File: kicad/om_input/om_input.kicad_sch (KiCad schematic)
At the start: 59 parts, among them J2 XLR3_AudioJack3_Combo_Switch, J3 Conn_01x08_Pin, Q1 PNP, Q2 PNP, SW1 SW_DPDT_x2, SW2 SW_4PDT_x4, U1 OPA1641, U2 OPA1612AxD, U3 OPA1612AxD, U4 OPA1612AxD, U5 OPA1612AxD

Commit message: gain and rails (#4)
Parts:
- added R28, R29, R30, R31: 1k, symbol Device:R_US
- R23: value 270 -> 100
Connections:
- net -9V: no longer D2.2 (A), D5.2 (A), J3.4 (Pin_4), R10.2, R15.2, U2.4 (V-), U4.4 (V-), U5.4 (V-)
- net Earth: now also R28.2, R29.1
- net at U3.1, U3.2 (-): now also R30.1; no longer R16.1
- net at U3.6 (-), U3.7: now also R31.1; no longer R17.1
- net at SW2.7 (A): now also R29.2, R31.2; no longer SW2.4 (A)
- net at SW2.8 (B): now also R17.1; no longer U3.5 (+)
- net -15V: now reaches U3.4 (V-)
- net -15V: now also D2.2 (A), D5.2 (A), J3.4 (Pin_4), R10.2, R15.2, U2.4 (V-), U4.4 (V-), U5.4 (V-)
- net +9V renamed +15V
- new net: R16.1, R28.1, R30.2
- new net: SW2.4 (A), U3.5 (+)
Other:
- note added: "(simulated approx. gain) stage 1 gain: +5dB to +35dB stage 2 gain: -4dB to +36dB stage 2 unbalanced gain: -10dB to +30dB mic/line pad: -6dB inst gain: 10dB mic gain: -5dB to +65db line gain: -10db to +30db inst gain: +0db to +40db"
- note removed: "(simulated approx. gain) stage 1 gain: +5db to +35db stage 2 gain: -4db to +27.5db stage 2 unbalanced gain: -10db to +21.5db inst gain: 10db mic gain: +1db to +62.5db line gain: -4db to +27.5db inst gain: +0db to +31.5db"
- moved on the sheet: C3, C5, C9, J2B, R26, R27, R5, R6, SW2A, SW2B, U1, U3A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

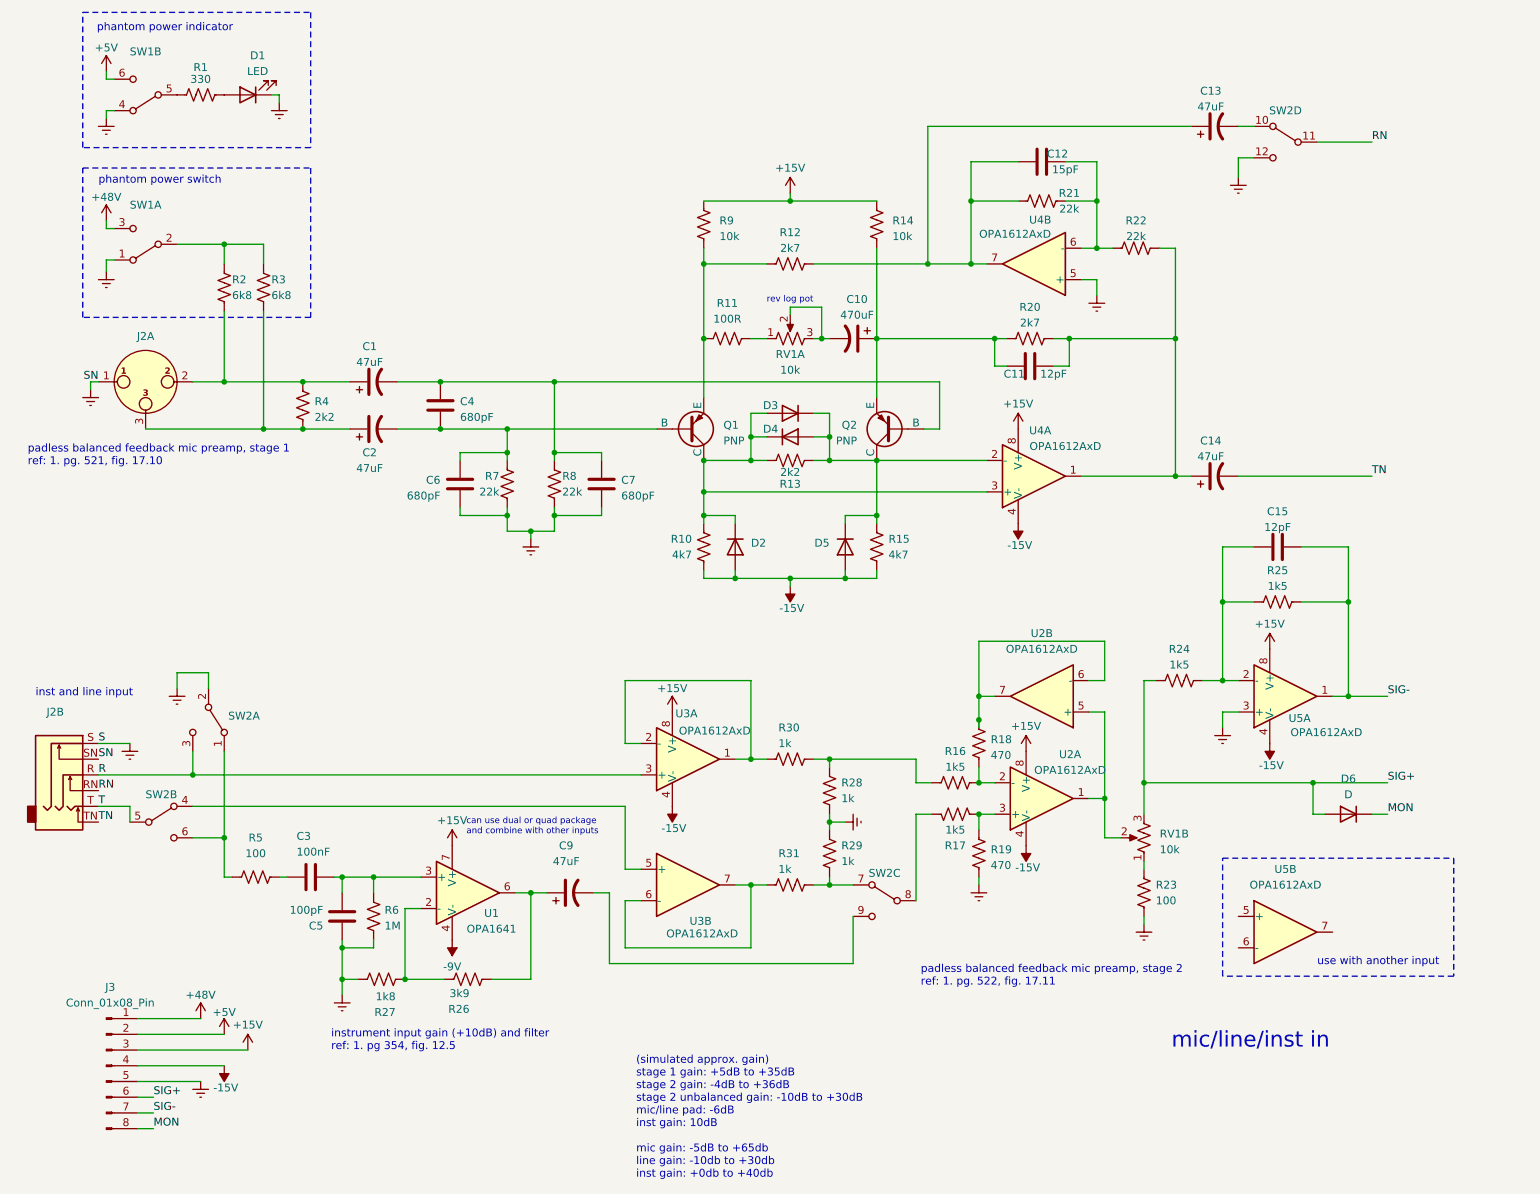
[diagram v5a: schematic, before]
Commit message: 5532's and TL072's everywhere
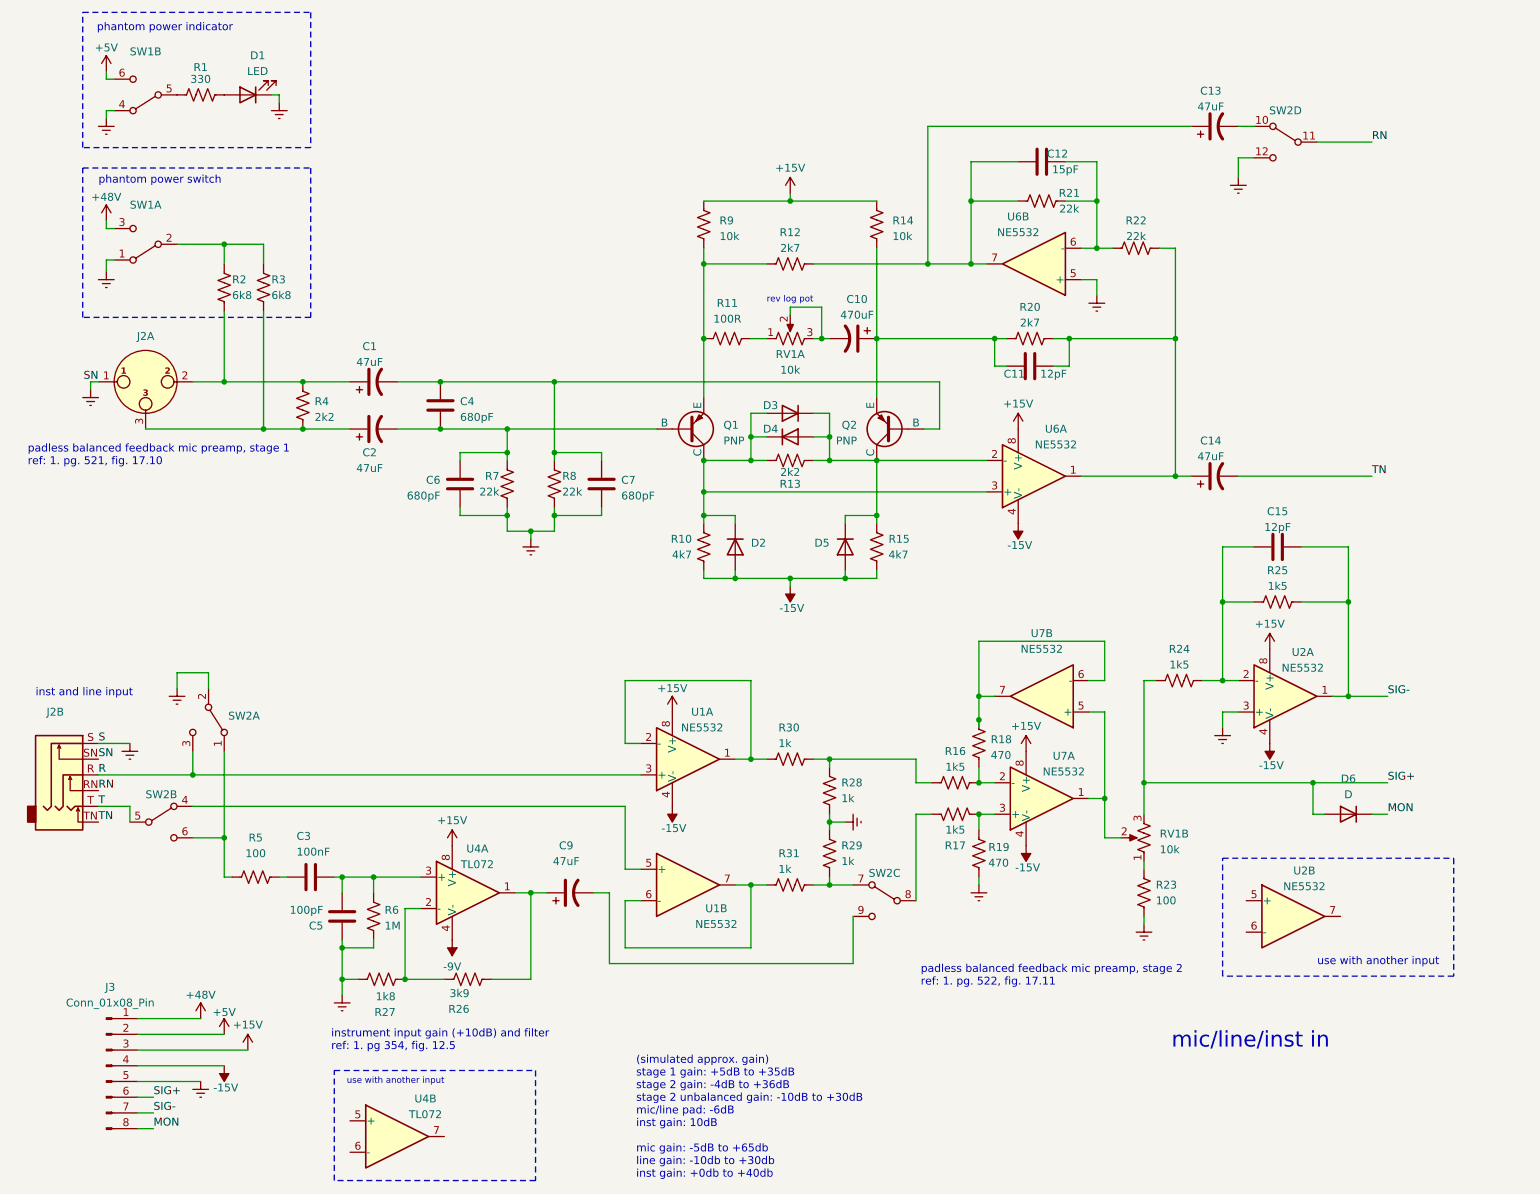
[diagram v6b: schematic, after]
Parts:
- removed U1: OPA1641, symbol Amplifier_Operational:OPA1641
- removed U2, U3, U4, U5: OPA1612AxD, symbol Amplifier_Operational:OPA1612AxD
- added U1, U2, U6, U7: NE5532, symbol Amplifier_Operational:NE5532
- added U4: TL072, symbol Amplifier_Operational:TL072
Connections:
- net +15V: now also U1.8 (V+), U2.8 (V+), U4.8 (V+), U6.8 (V+), U7.8 (V+)
- net -15V: now also U1.4 (V-), U2.4 (V-), U6.4 (V-), U7.4 (V-)
- net -9V: now also U4.4 (V-)
- net Earth: now also U2.3 (+), U6.5 (+)
- net R: now also U1.3 (+)
- net SIG-: now also U2.1
- net at R30.1: now also U1.1, U1.2 (-)
- net at R17.2, R19.1: now also U7.3 (+)
- net at R26.2, R27.1: now also U4.2 (-)
- net at C9.1, R26.1: now also U4.1
- net at D3.1 (K), D4.2 (A), D5.1 (K)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: now also U6.2 (-)
- net at R18.1: now also U7.6 (-), U7.7
- net at R16.2, R18.2: now also U7.2 (-)
- net at C15.1, R24.2, R25.1: now also U2.2 (-)
- net at D2.1 (K), D3.2 (A), D4.1 (K)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: now also U6.3 (+)
- net at R31.1: now also U1.6 (-), U1.7
- net at C12.1, C13.1, R12.2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: now also U6.7
- net at C12.2, R21.2, R22.1: now also U6.6 (-)
- net at C3.2, C5.2, R6.2: now also U4.3 (+)
- net at RV1.2: now also U7.1, U7.5 (+)
- net at SW2.4 (A): now also U1.5 (+)
- net at C11.2, C14.1, R20.2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: now also U6.1
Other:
- note removed: "can use dual or quad package and combine with other inputs"

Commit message: phantom power
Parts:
- renumbered C3 to C1, C11 to C10, C12 to C11, C13 to C12, C14 to C13, C15 to C14, C5 to C2, C1 to C3, C2 to C4, C4 to C5, C9 to C7, C7 to C8, C10 to C9, J2 to J1, J3 to J2, R8 to R10, R9 to R11, R10 to R12, R11 to R13, R12 to R14, R13 to R15, R30 to R16, R31 to R17, R28 to R18, R29 to R19, R14 to R20, R15 to R21, R16 to R22, R17 to R23, R18 to R24, R19 to R25, R20 to R26, R21 to R27, R22 to R28, R23 to R29, R5 to R3, R24 to R30, R25 to R31, R3 to R4, R4 to R5, R27 to R7, R26 to R8, R7 to R9, U4 to U1, U1 to U2, U6 to U3, U7 to U4, U2 to U5
